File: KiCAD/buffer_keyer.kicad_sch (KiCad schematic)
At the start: 75 parts, among them J1 Conn_01x02_Pin, J13 Conn_01x05, J2 Conn_01x02_Pin, J3 Conn_01x02_Pin, T1 2N3906, T2 2N3906, U19 L79L08_TO92, U20 ICL7660S, U3 MC1496, U4 MCP4921, U6 LM7171xIN, U7 LM7171xIN, U8 MCP4728

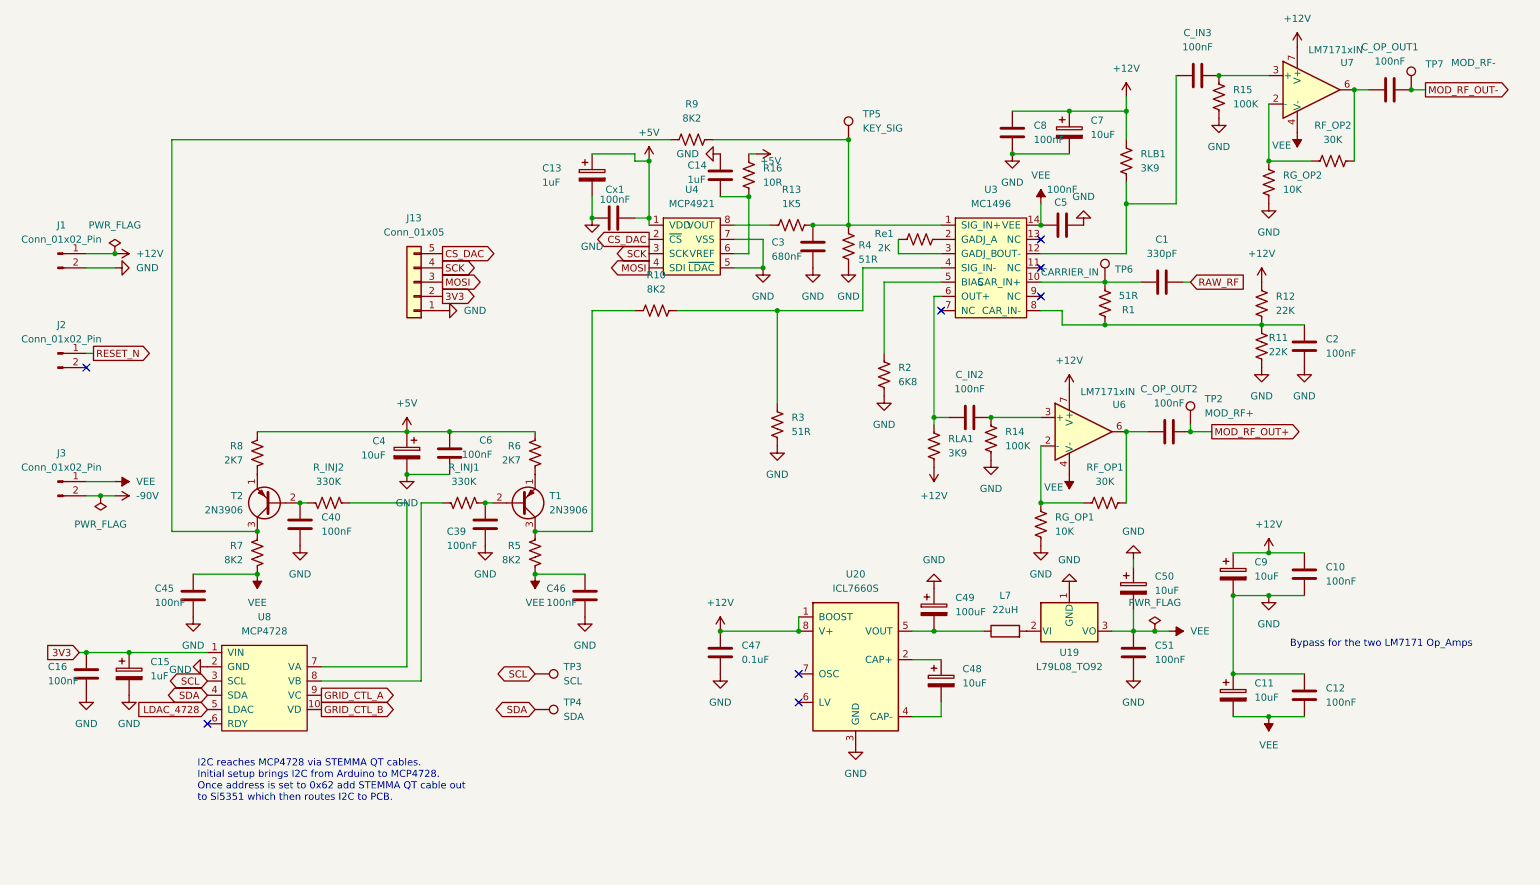
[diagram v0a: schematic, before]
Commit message: kicad: buffer_keyer LM7805 local, J3 to bias, more testpoints
- buffer_keyer.kicad_sch: LM7805 5V regulator + bypass caps copied over
  from bias sheet so this board only needs +12V input. Multiple new
  testpoints added: T1/T2 collectors, LDAC (near U8), DAC output (near
  U4), and one placeholder. Signals now covered end-to-end for
  envelope + modulator debugging.
- bias.kicad_sch: J3 relocated here (was on buffer_keyer). J3 pin 1
  VEE previously conflicted with the new local VEE generator on
  buffer_keyer -- moving J3 to bias also means it belongs on the
  bias board once that becomes its own PCB. VEE pin will be
  repurposed as GND on that side.
- arduino.kicad_sch: incidental annotation edits.

Architectural decision recorded (not yet acted on): bias will become
a separate PCB, both boards in the same top-mount subchassis, ribbon
between them, only the four tube-facing signals (GRID_BIAS_A/B_OUT,
CATHODE_SENSE_A/B) cross into the main chassis via a round bulkhead.
I_CATHODE_A/B and GRID_BLOCK_CRASH will reach the Metro via direct
jumpers from bias-PCB header pins (Path B), not through the ribbon.

Co-Authored-By: Claude Opus 4.7 <noreply@anthropic.com>
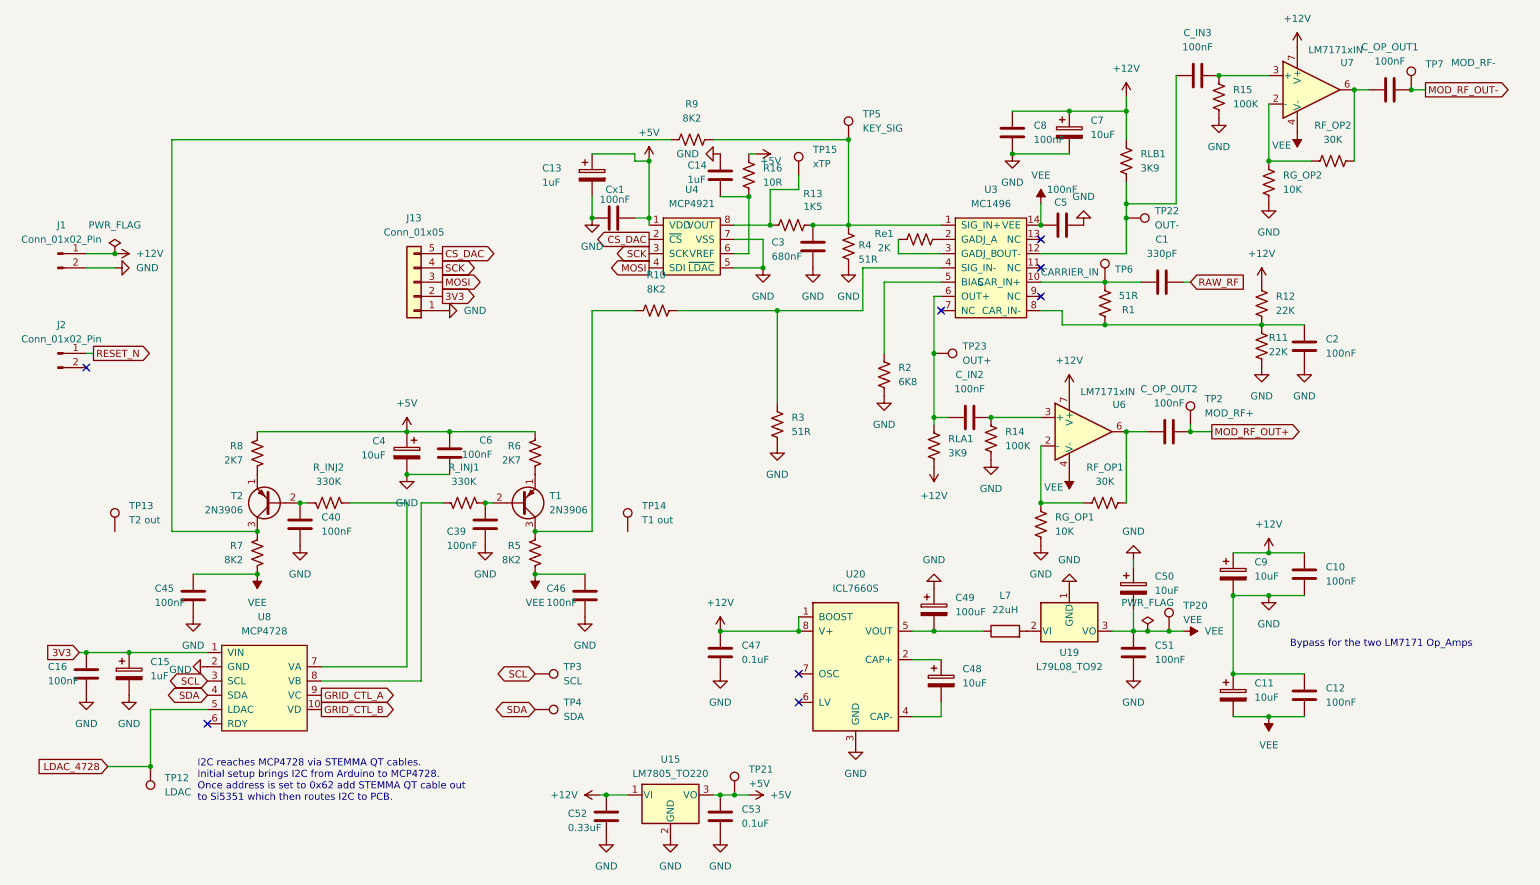
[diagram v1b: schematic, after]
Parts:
- removed J3: Conn_01x02_Pin, Connector_PinHeader_2.54mm:PinHeader_1x02_P2.54mm_Vertical, symbol Connector:Conn_01x02_Pin
- added C52: 0.33uF, Capacitor_THT:C_Rect_L7.0mm_W3.5mm_P5.00mm, symbol Device:C
- added C53: 0.1uF, Capacitor_THT:C_Disc_D5.0mm_W2.5mm_P5.00mm, symbol Device:C
- added TP12: LDAC, Connector_PinHeader_2.54mm:PinHeader_1x01_P2.54mm_Vertical, symbol xmitter:xTP
- added TP13: T2 out, Connector_PinHeader_2.54mm:PinHeader_1x01_P2.54mm_Vertical, symbol xmitter:xTP
- added TP14: T1 out, Connector_PinHeader_2.54mm:PinHeader_1x01_P2.54mm_Vertical, symbol xmitter:xTP
- added TP15: xTP, Connector_PinHeader_2.54mm:PinHeader_1x01_P2.54mm_Vertical, symbol xmitter:xTP
- added TP20: VEE, Connector_PinHeader_2.54mm:PinHeader_1x01_P2.54mm_Vertical, symbol xmitter:xTP
- added TP21: +5V, Connector_PinHeader_2.54mm:PinHeader_1x01_P2.54mm_Vertical, symbol xmitter:xTP
- added TP22: OUT-, Connector_PinHeader_2.54mm:PinHeader_1x01_P2.54mm_Vertical, symbol xmitter:xTP
- added TP23: OUT+, Connector_PinHeader_2.54mm:PinHeader_1x01_P2.54mm_Vertical, symbol xmitter:xTP
- added U15: LM7805_TO220, Package_TO_SOT_THT:TO-220-3_Vertical, symbol Regulator_Linear:LM7805_TO220
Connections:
- net +12V: now also C52.1, U15.1 (VI)
- net +5V: now also C53.1, TP21.1, U15.3 (VO)
- net GND: now also C52.2, C53.2, U15.2 (GND)
- net LDAC_4728: now also TP12.1
- net VEE: now also TP20.1
- net at C_IN2.1, RLA1.2, U3.6 (OUT+): now also TP23.1
- net at C_IN3.1, RLB1.2, U3.12 (OUT-): now also TP22.1
- net at R13.1, U4.8 (VOUT): now also TP15.1

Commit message: kicad: buffer_keyer part placement complete; component datasheets
- KiCAD.kicad_pcb: placement for VEE generator (U15, U19, C47-C51, L7),
  local LM7805 + bypass caps, and new test points on buffer_keyer
- arduino/buffer_keyer schematics: minor cleanup from PCB update pass
- Documentation/Components: add 78F series, L79L, ICL7660S-A, Wurth
  Elek-caap datasheets for reference

Co-Authored-By: Claude Opus 4.7 <noreply@anthropic.com>
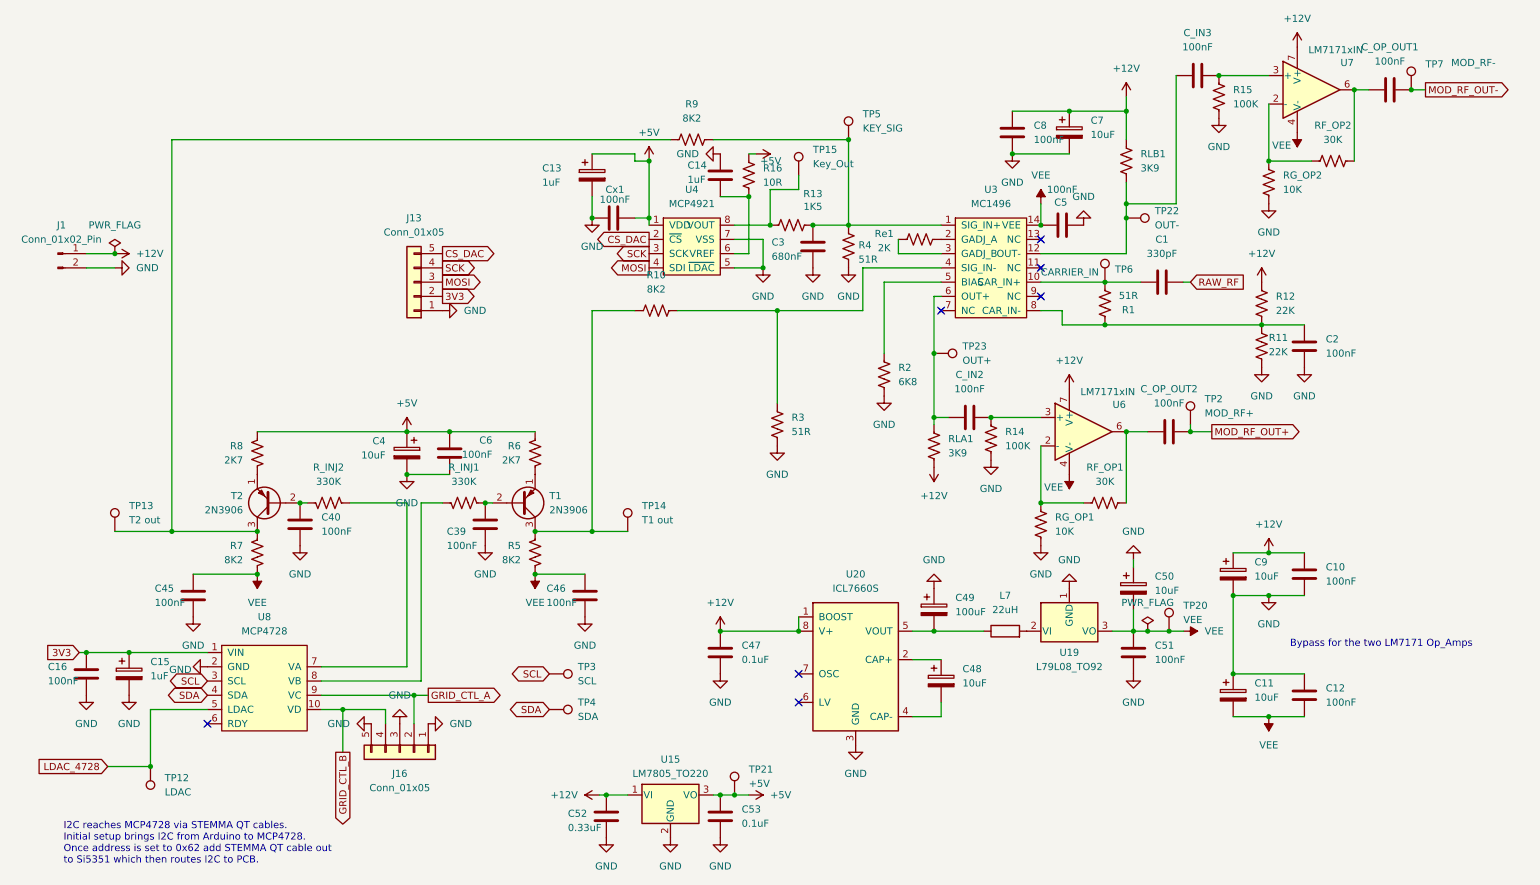
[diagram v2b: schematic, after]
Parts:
- removed J2: Conn_01x02_Pin, Connector_PinHeader_2.54mm:PinHeader_1x02_P2.54mm_Vertical, symbol Connector:Conn_01x02_Pin
- added J16: Conn_01x05, Connector_PinHeader_2.54mm:PinHeader_1x05_P2.54mm_Vertical, symbol Connector_Generic:Conn_01x05
- C47, C51: footprint (none) -> Capacitor_THT:C_Disc_D5.0mm_W2.5mm_P5.00mm
- C48, C50: footprint (none) -> Capacitor_THT:CP_Radial_D5.0mm_P2.00mm
- C49: footprint (none) -> Capacitor_THT:CP_Radial_D6.3mm_P2.50mm
- L7: footprint (none) -> Inductor_THT:L_Axial_L7.0mm_D3.3mm_P10.16mm_Horizontal_Fastron_MICC
- TP15: value xTP -> Key_Out
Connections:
- net GND: now also J16.1 (Pin_1), J16.3 (Pin_3), J16.5 (Pin_5)
- net GRID_CTL_A: now also J16.2 (Pin_2)
- net GRID_CTL_B: now also J16.4 (Pin_4)
- net at R10.1, R5.1, T1.3 (C): now also TP14.1
- net at R7.1, R9.1, T2.3 (C): now also TP13.1
- no-connect marks 8 -> 7
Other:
- moved on the sheet: TP3, TP4

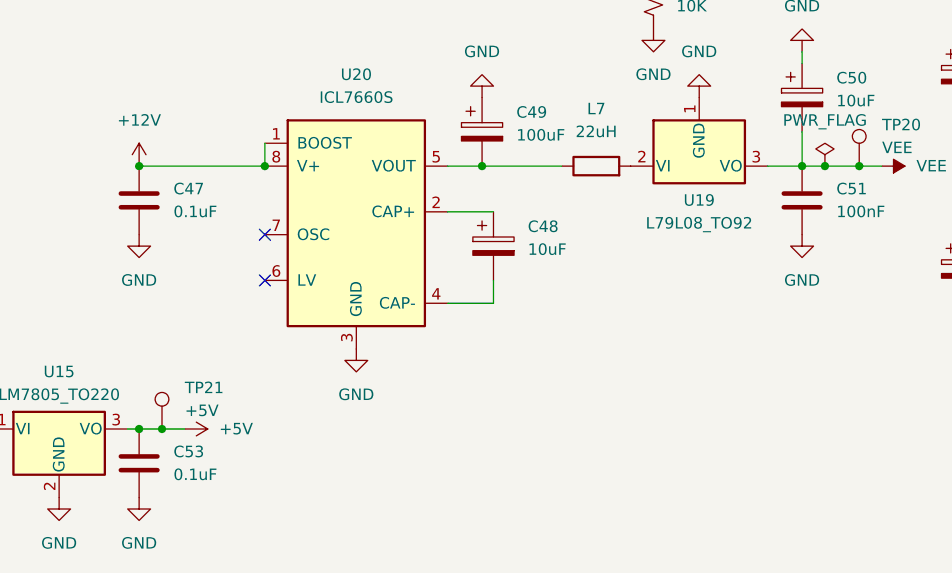
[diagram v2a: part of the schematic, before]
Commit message: kicad: L79L08 local decoupling; unlink bias sheet from root
- Add C17/C18 (0.33 uF Z5U SR205E334MAR) at L79L08 in/out to prevent
  oscillation and damp L7+U19 ringing
- New footprint xmitter:Kyocera_SR20_MLCC for the SR20 style radial MLCC
  (2.54 mm pitch, 5.08 x 3.175 mm body)
- Add SR-Series datasheet to Documentation/Components
- Unlink bias sheet from root schematic — first step in splitting the
  bias circuit onto its own PCB

Co-Authored-By: Claude Opus 4.7 <noreply@anthropic.com>
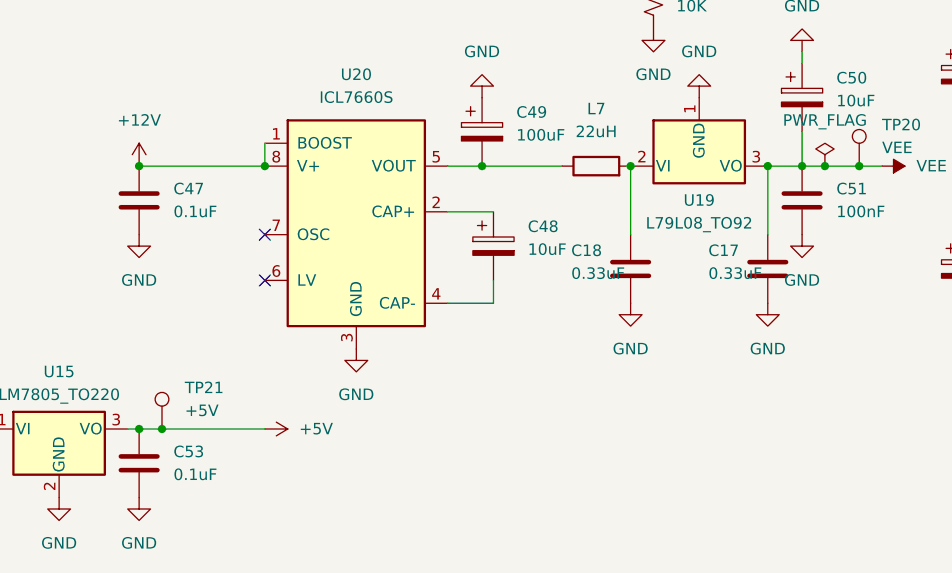
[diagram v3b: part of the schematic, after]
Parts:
- added C17, C18: 0.33uF, xmitter:Kyocera_SR20_MLCC, symbol Device:C
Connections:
- net GND: now also C17.2, C18.2
- net VEE: now also C17.1
- net at L7.2, U19.2 (VI): now also C18.1
